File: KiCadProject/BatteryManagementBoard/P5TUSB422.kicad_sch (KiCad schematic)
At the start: 8 parts, among them U501 PTN5150

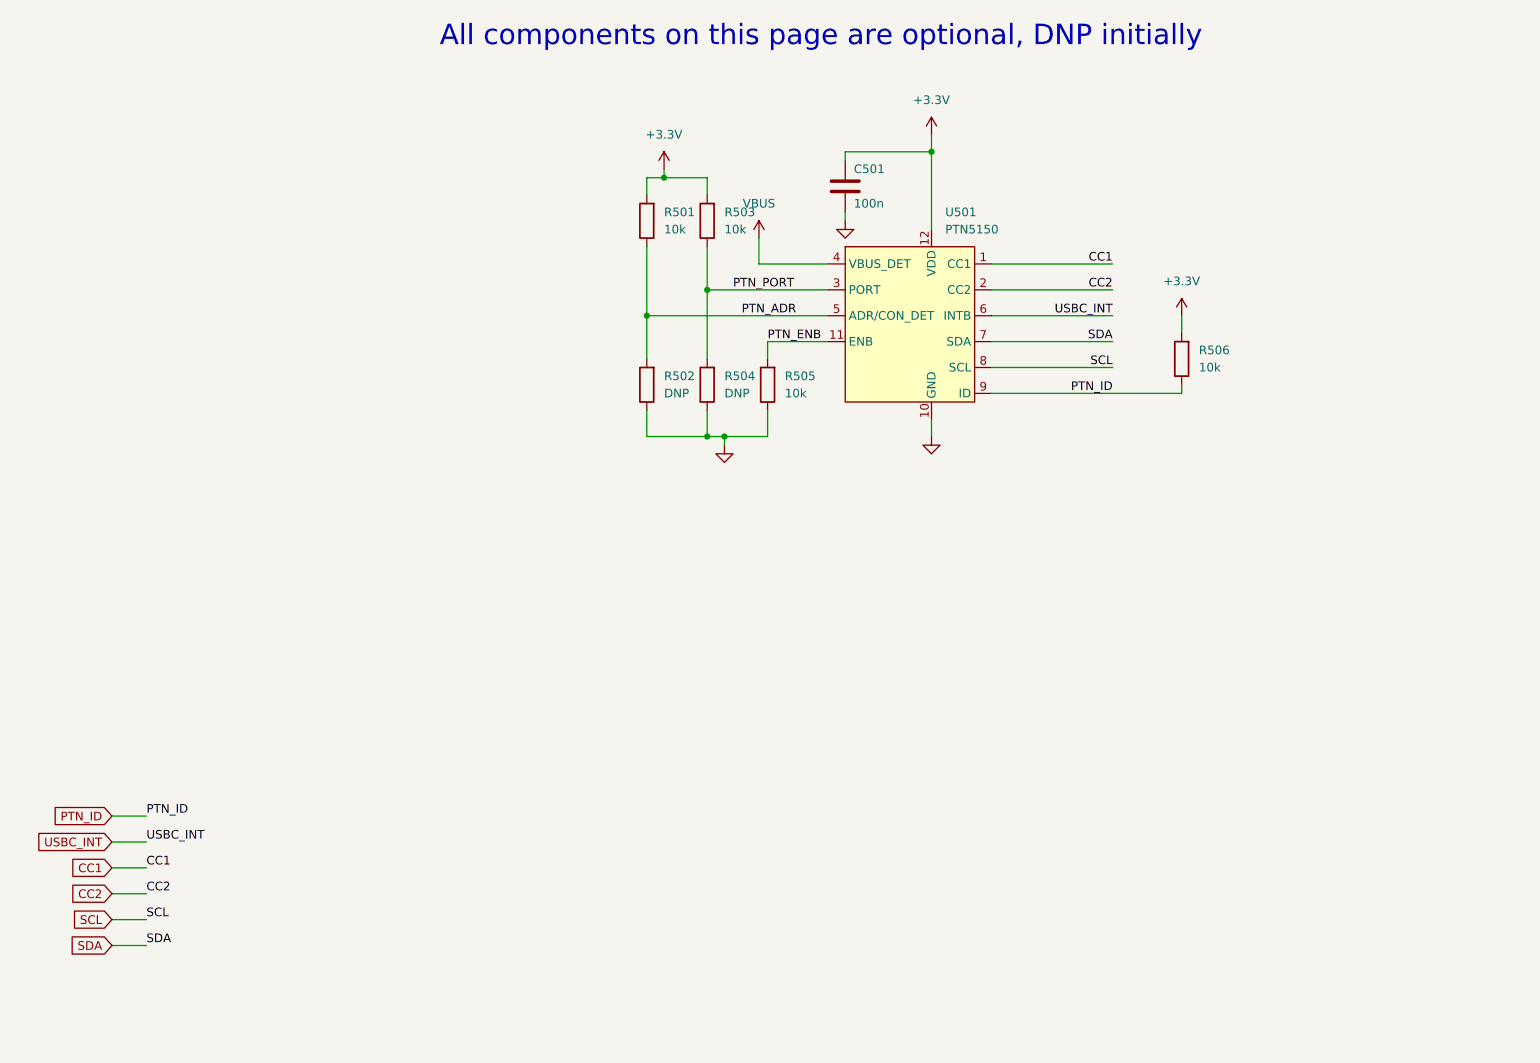
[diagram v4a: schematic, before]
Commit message: All PCB's should be done. Do a final check before ordering.
Signed-off-by: Eldalote.Electronics <Eldalote.Electronics@gmail.com>
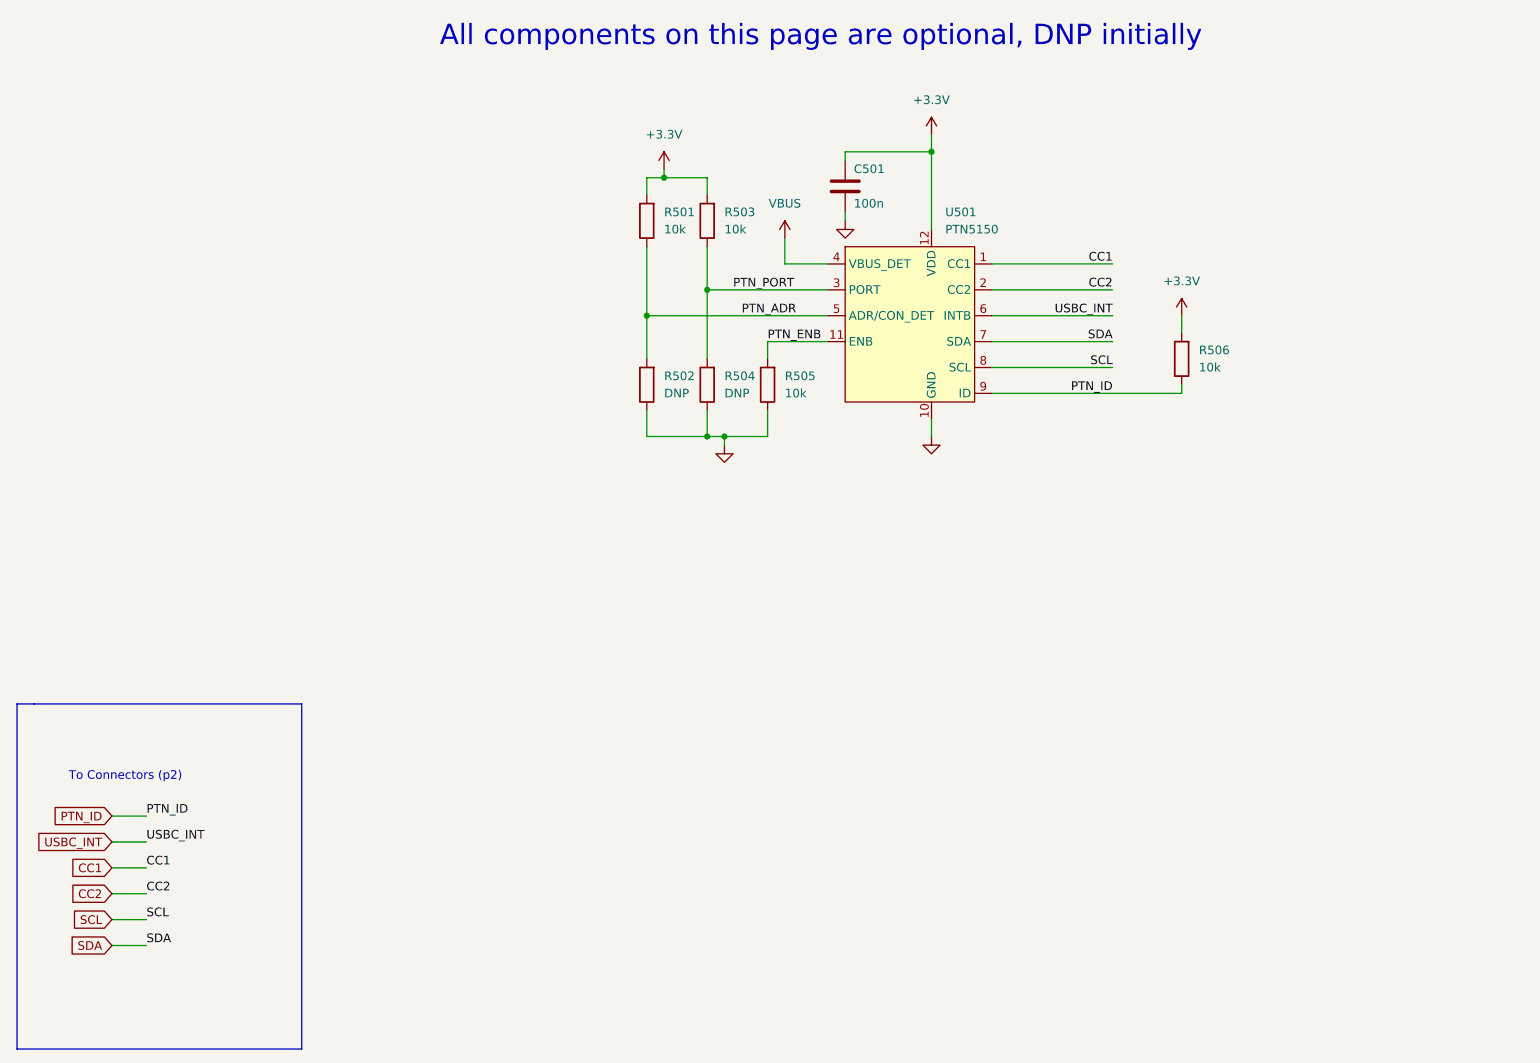
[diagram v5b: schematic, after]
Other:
- note added: "To Connectors (p2)"
- company: (none) -> Eldalote Electronics
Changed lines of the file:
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@@
 (kicad_sch (version 20211123) (generator eeschema)
   (paper "A4")
+  (title_block
+    (rev "0.3")
+    (company "Eldalote Electronics")
+  )
   (junction (at 120.65 78.74) (diameter 0) (color 0 0 0 0)
   )
@@
     (stroke (width 0) (type default) (color 0 0 0 0))
   )
+  (polyline (pts (xy 60.96 139.7) (xy 60.96 190.5))
+    (stroke (width 0) (type default) (color 0 0 0 0))
+  )
   (wire (pts (xy 33.02 156.21) (xy 38.1 156.21))
     (stroke (width 0) (type default) (color 0 0 0 0))
@@
     (stroke (width 0) (type default) (color 0 0 0 0))
   )
+  (polyline (pts (xy 19.05 139.7) (xy 21.59 139.7))
+    (stroke (width 0) (type default) (color 0 0 0 0))
+  )
   (wire (pts (xy 120.65 62.23) (xy 120.65 64.77))
     (stroke (width 0) (type default) (color 0 0 0 0))
@@
     (stroke (width 0) (type default) (color 0 0 0 0))
   )
+  (polyline (pts (xy 60.96 190.5) (xy 19.05 190.5))
+    (stroke (width 0) (type default) (color 0 0 0 0))
+  )
   (wire (pts (xy 114.3 62.23) (xy 111.76 62.23))
     (stroke (width 0) (type default) (color 0 0 0 0))
@@
     (stroke (width 0) (type default) (color 0 0 0 0))
   )
+  (polyline (pts (xy 19.05 190.5) (xy 19.05 139.7))
+    (stroke (width 0) (type default) (color 0 0 0 0))
+  )
   (wire (pts (xy 120.65 62.23) (xy 114.3 62.23))
     (stroke (width 0) (type default) (color 0 0 0 0))
@@
     (stroke (width 0) (type default) (color 0 0 0 0))
   )
-  (wire (pts (xy 128.27 74.93) (xy 138.43 74.93))
+  (wire (pts (xy 132.08 74.93) (xy 138.43 74.93))
     (stroke (width 0) (type default) (color 0 0 0 0))
   )
@@
     (stroke (width 0) (type default) (color 0 0 0 0))
   )
+  (polyline (pts (xy 21.59 139.7) (xy 60.96 139.7))
+    (stroke (width 0) (type default) (color 0 0 0 0))
+  )
   (wire (pts (xy 162.56 90.17) (xy 180.34 90.17))
     (stroke (width 0) (type default) (color 0 0 0 0))
@@
     (stroke (width 0) (type default) (color 0 0 0 0))
   )
-  (wire (pts (xy 128.27 71.12) (xy 128.27 74.93))
+  (wire (pts (xy 132.08 71.12) (xy 132.08 74.93))
     (stroke (width 0) (type default) (color 0 0 0 0))
   )
@@
     (effects (font (size 3 3)) (justify left bottom))
   )
+  (text "To Connectors (p2)\n" (at 26.67 151.13 0)
+    (effects (font (size 1.27 1.27)) (justify left bottom))
+  )
   (label "SCL" (at 38.1 171.45 0)
     (effects (font (size 1.27 1.27)) (justify left bottom))
@@
     (pin "2")
   )
-  (symbol (lib_id "power:VBUS") (at 128.27 71.12 0) (unit 1)
+  (symbol (lib_id "power:VBUS") (at 132.08 71.12 0) (unit 1)
     (in_bom yes) (on_board yes) (fields_autoplaced)
-    (property "Reference" "#PWR0502" (id 0) (at 128.27 74.93 0)
-      (effects (font (size 1.27 1.27)) hide)
-    )
-    (property "Value" "VBUS" (id 1) (at 128.27 66.04 0))
-    (property "Footprint" "" (id 2) (at 128.27 71.12 0)
-      (effects (font (size 1.27 1.27)) hide)
-    )
-    (property "Datasheet" "" (id 3) (at 128.27 71.12 0)
-      (effects (font (size 1.27 1.27)) hide)
-    )
+    (property "Reference" "#PWR0502" (id 0) (at 132.08 74.93 0)
+      (effects (font (size 1.27 1.27)) hide)
+    )
+    (property "Value" "VBUS" (id 1) (at 132.08 66.04 0))
+    (property "Footprint" "" (id 2) (at 132.08 71.12 0)
+      (effects (font (size 1.27 1.27)) hide)
+    )
+    (property "Datasheet" "" (id 3) (at 132.08 71.12 0)
+      (effects (font (size 1.27 1.27)) hide)
+    )
